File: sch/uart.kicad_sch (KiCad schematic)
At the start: 16 parts, among them J501 USB_B_Mini, U501 FT230XS

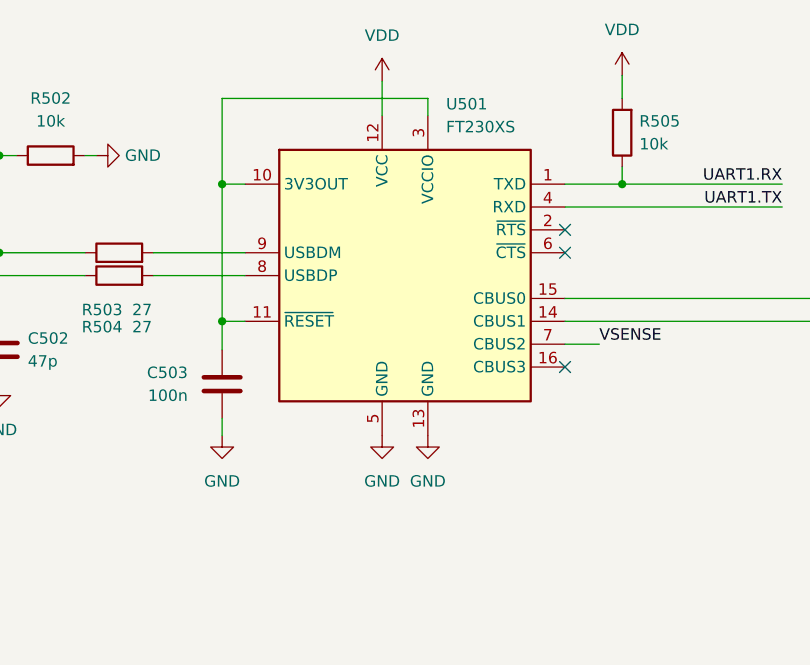
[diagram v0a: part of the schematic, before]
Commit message: Replaced FTDI package with QFN one
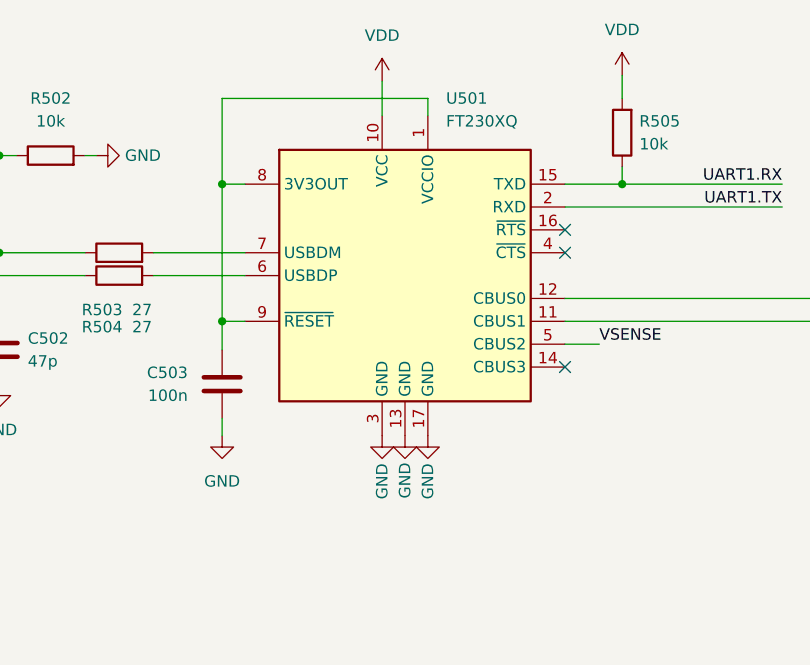
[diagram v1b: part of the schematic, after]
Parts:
- removed U501: FT230XS, Package_SO:SSOP-16_3.9x4.9mm_P0.635mm, symbol Interface_USB:FT230XS
- added U501: FT230XQ, Package_DFN_QFN:QFN-16-1EP_4x4mm_P0.65mm_EP2.1x2.1mm, symbol Interface_USB:FT230XQ
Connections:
- net GND: now also U501.13 (GND), U501.17 (GND), U501.3 (GND)
- net UART1.RX: now also U501.15 (TXD)
- net UART1.TX: now also U501.2 (RXD)
- net VDD: now also U501.10 (VCC)
- net VSENSE: now also U501.5 (CBUS2)
- net at C503.1: now also U501.1 (VCCIO), U501.8 (3V3OUT), U501.9 (~{RESET})
- net at R507.1: now also U501.11 (CBUS1)
- net at R506.1: now also U501.12 (CBUS0)
- net at R504.2: now also U501.6 (USBDP)
- net at R503.2: now also U501.7 (USBDM)

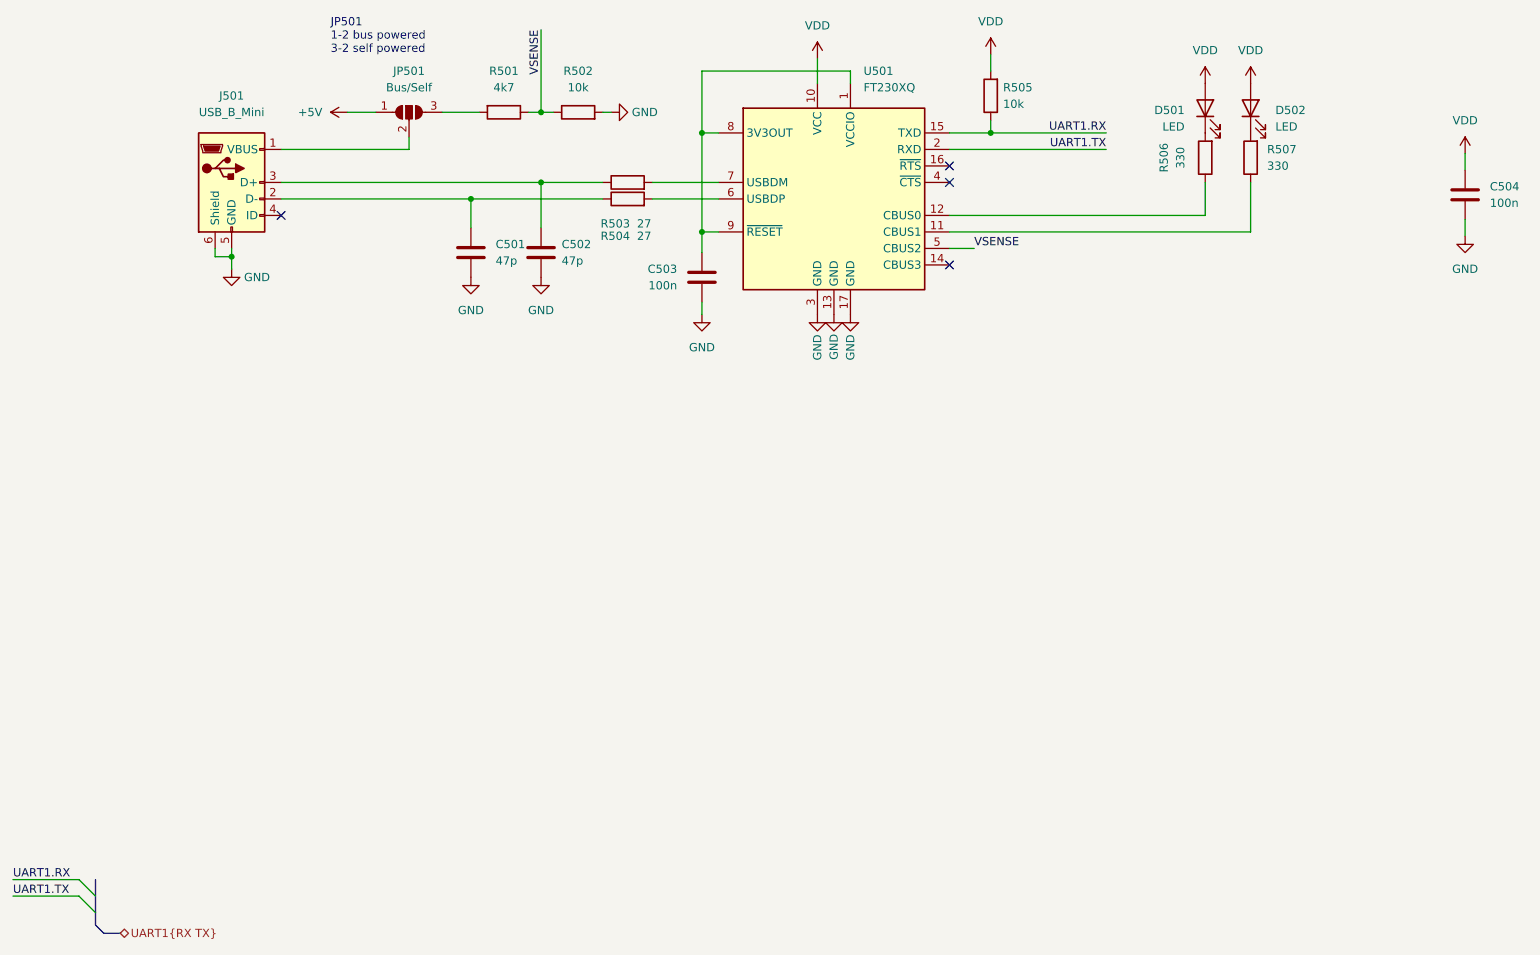
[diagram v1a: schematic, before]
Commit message: Added more expansion capability.
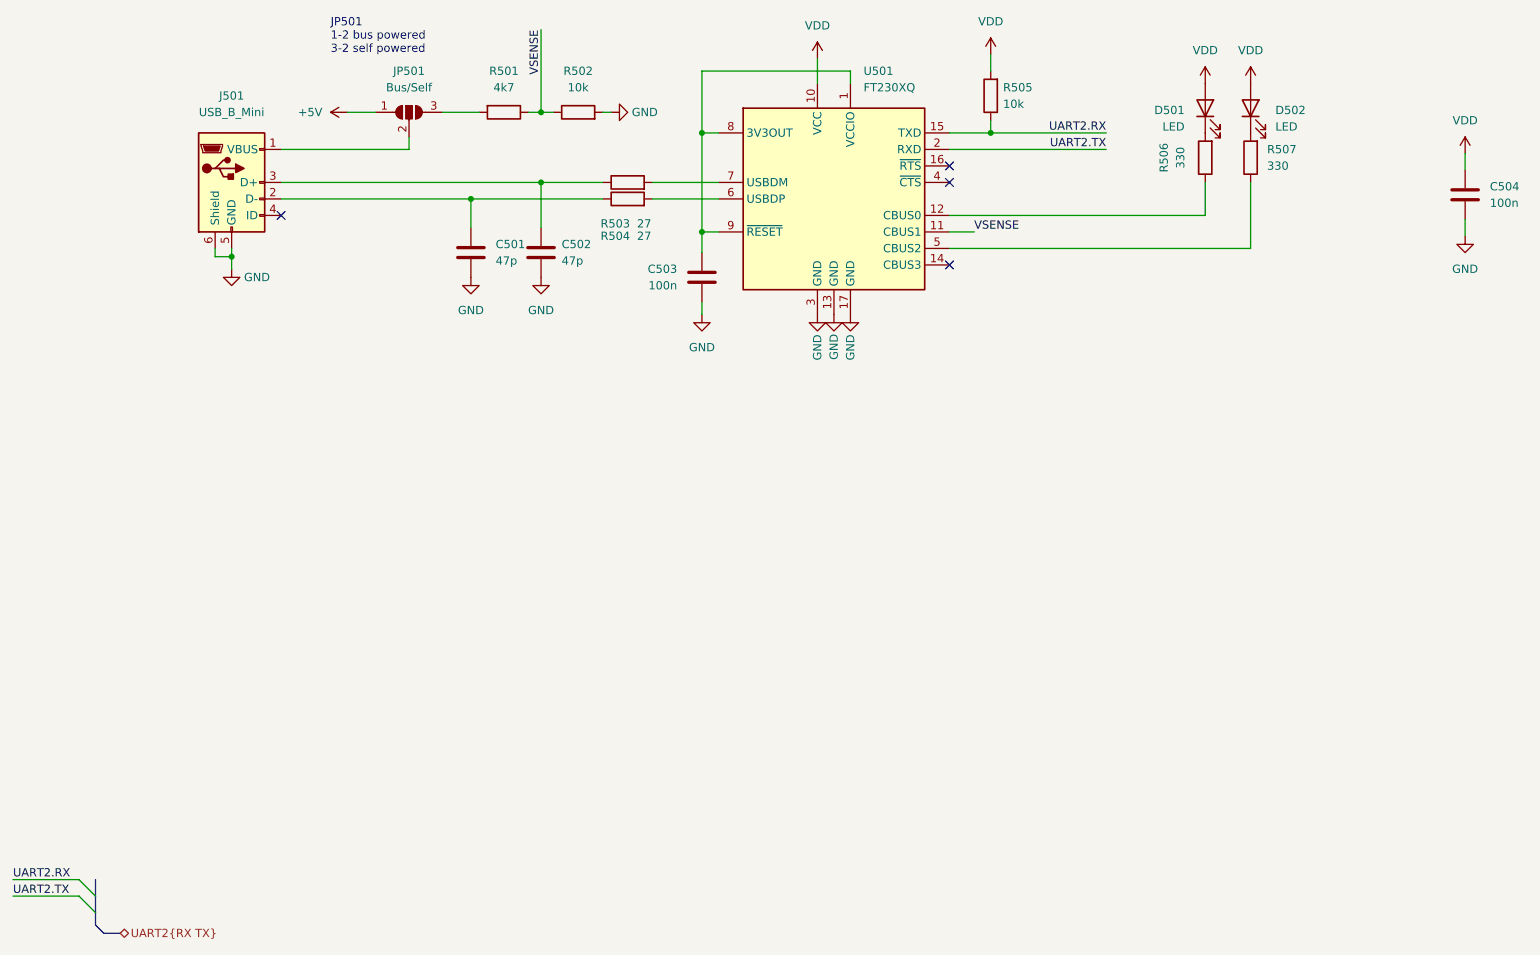
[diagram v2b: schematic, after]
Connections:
- net VSENSE: now also U501.11 (CBUS1); no longer U501.5 (CBUS2)
- net at R507.1: now also U501.5 (CBUS2); no longer U501.11 (CBUS1)
- net UART1.RX renamed UART2.RX
- net UART1.TX renamed UART2.TX
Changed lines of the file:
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@@
     (stroke (width 0) (type default) (color 0 0 0 0))
   )
-  (wire (pts (xy 207.645 84.455) (xy 207.645 76.835))
+  (wire (pts (xy 207.645 76.835) (xy 207.645 86.995))
     (stroke (width 0) (type default) (color 0 0 0 0))
   )
@@
   )
   (wire (pts (xy 240.665 82.55) (xy 240.665 85.09))
-    (stroke (width 0) (type default) (color 0 0 0 0))
-  )
-  (wire (pts (xy 161.29 84.455) (xy 207.645 84.455))
     (stroke (width 0) (type default) (color 0 0 0 0))
   )
@@
     (stroke (width 0) (type default) (color 0 0 0 0))
   )
+  (wire (pts (xy 161.29 86.995) (xy 207.645 86.995))
+    (stroke (width 0) (type default) (color 0 0 0 0))
+  )
   (wire (pts (xy 87.63 79.375) (xy 107.95 79.375))
     (stroke (width 0) (type default) (color 0 0 0 0))
@@
     (stroke (width 0) (type default) (color 0 0 0 0))
   )
-  (wire (pts (xy 161.29 86.995) (xy 165.1 86.995))
+  (wire (pts (xy 161.29 84.455) (xy 165.1 84.455))
     (stroke (width 0) (type default) (color 0 0 0 0))
   )
@@
     (effects (font (size 1.27 1.27)) (justify left bottom))
   )
-  (label "VSENSE" (at 165.1 86.995 0)
+  (label "VSENSE" (at 165.1 84.455 0)
     (effects (font (size 1.27 1.27)) (justify left bottom))
   )
-  (label "UART1.TX" (at 185.42 71.755 180)
+  (label "UART2.TX" (at 185.42 71.755 180)
     (effects (font (size 1.27 1.27)) (justify right bottom))
   )
-  (label "UART1.TX" (at 17.145 186.69 0)
+  (label "UART2.TX" (at 17.145 186.69 0)
     (effects (font (size 1.27 1.27)) (justify left bottom))
   )
-  (label "UART1.RX" (at 185.42 69.215 180)
+  (label "UART2.RX" (at 185.42 69.215 180)
     (effects (font (size 1.27 1.27)) (justify right bottom))
   )
@@
     (effects (font (size 1.27 1.27)) (justify right bottom))
   )
-  (label "UART1.RX" (at 17.145 184.15 0)
+  (label "UART2.RX" (at 17.145 184.15 0)
     (effects (font (size 1.27 1.27)) (justify left bottom))
   )
-  (hierarchical_label "UART1{RX TX}" (shape bidirectional) (at 33.655 192.405 0)
+  (hierarchical_label "UART2{RX TX}" (shape bidirectional) (at 33.655 192.405 0)
     (effects (font (size 1.27 1.27)) (justify left))
   )
